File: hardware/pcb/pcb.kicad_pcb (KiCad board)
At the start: 2 copper layers, 26.7 x 56.6 mm, 30 parts, among them J1 L_GPIO, J2 R_GPIO, J3 USB_C_Receptacle_USB2.0_14P, U1 ESP32-C3-WROOM-02, U3 TPS62291

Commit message: I dont remeber, something with PCB :)
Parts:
- BOOT: footprint TestPoint:TestPoint_Pad_2.0x2.0mm -> TestPoint:TestPoint_Pad_D1.5mm
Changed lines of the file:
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@@
 	(net 48 "/SFDLED")
 	(net 49 "/TXLED")
-	(net 50 "Net-(R3-Pad1)")
-	(net 51 "unconnected-(D5-DOUT-Pad2)")
-	(net 52 "Net-(J3-CC1)")
-	(net 53 "Net-(J3-CC2)")
-	(net 54 "Net-(D-RX1-A)")
-	(net 55 "Net-(D-RXOK1-A)")
-	(net 56 "Net-(D-SFD1-A)")
-	(net 57 "Net-(D-TX1-A)")
+	(net 50 "unconnected-(D5-DOUT-Pad2)")
+	(net 51 "Net-(J3-CC1)")
+	(net 52 "Net-(J3-CC2)")
+	(net 53 "Net-(D-RX1-A)")
+	(net 54 "Net-(D-RXOK1-A)")
+	(net 55 "Net-(D-SFD1-A)")
+	(net 56 "Net-(D-TX1-A)")
+	(net 57 "Net-(BOOT1-Pad1)")
 	(footprint "LED_SMD:LED_0402_1005Metric"
 		(layer "F.Cu")
@@
 			(layers "F.Cu" "F.Mask" "F.Paste")
 			(roundrect_rratio 0.25)
-			(net 56 "Net-(D-SFD1-A)")
+			(net 55 "Net-(D-SFD1-A)")
 			(pinfunction "A")
 			(pintype "passive")
@@
 			(layers "F.Cu" "F.Mask" "F.Paste")
 			(roundrect_rratio 0.25)
-			(net 55 "Net-(D-RXOK1-A)")
+			(net 54 "Net-(D-RXOK1-A)")
 			(pinfunction "A")
 			(pintype "passive")
@@
 			(layers "F.Cu" "F.Mask" "F.Paste")
 			(roundrect_rratio 0.1)
-			(net 51 "unconnected-(D5-DOUT-Pad2)")
+			(net 50 "unconnected-(D5-DOUT-Pad2)")
 			(pinfunction "DOUT")
 			(pintype "output")
@@
 			(layers "F.Cu" "F.Mask" "F.Paste")
 			(roundrect_rratio 0.25)
-			(net 52 "Net-(J3-CC1)")
+			(net 51 "Net-(J3-CC1)")
 			(pintype "passive")
 		)
@@
 			(layers "F.Cu" "F.Mask" "F.Paste")
 			(roundrect_rratio 0.25)
-			(net 56 "Net-(D-SFD1-A)")
+			(net 55 "Net-(D-SFD1-A)")
 			(pintype "passive")
 		)
@@
 			(layers "F.Cu" "F.Mask" "F.Paste")
 			(roundrect_rratio 0.25)
-			(net 57 "Net-(D-TX1-A)")
+			(net 56 "Net-(D-TX1-A)")
 			(pinfunction "A")
 			(pintype "passive")
@@
 			(size 0.3 1.24)
 			(layers "F.Cu" "F.Mask" "F.Paste")
-			(net 52 "Net-(J3-CC1)")
+			(net 51 "Net-(J3-CC1)")
 			(pinfunction "CC1")
 			(pintype "bidirectional")
@@
 			(size 0.3 1.24)
 			(layers "F.Cu" "F.Mask" "F.Paste")
-			(net 53 "Net-(J3-CC2)")
+			(net 52 "Net-(J3-CC2)")
 			(pinfunction "CC2")
 			(pintype "bidirectional")
@@
 			(layers "F.Cu" "F.Mask" "F.Paste")
 			(roundrect_rratio 0.25)
-			(net 55 "Net-(D-RXOK1-A)")
+			(net 54 "Net-(D-RXOK1-A)")
 			(pintype "passive")
 		)
@@
 			(layers "F.Cu" "F.Mask" "F.Paste")
 			(roundrect_rratio 0.25)
-			(net 57 "Net-(D-TX1-A)")
+			(net 56 "Net-(D-TX1-A)")
 			(pintype "passive")
 		)
@@
 			(layers "F.Cu" "F.Mask" "F.Paste")
 			(roundrect_rratio 0.25)
-			(net 50 "Net-(R3-Pad1)")
+			(net 57 "Net-(BOOT1-Pad1)")
 			(pintype "passive")
 		)
@@
 			(layers "F.Cu" "F.Mask" "F.Paste")
 			(roundrect_rratio 0.25)
-			(net 54 "Net-(D-RX1-A)")
+			(net 53 "Net-(D-RX1-A)")
 			(pinfunction "A")
 			(pintype "passive")
@@
 			(layers "F.Cu" "F.Mask" "F.Paste")
 			(roundrect_rratio 0.25)
-			(net 53 "Net-(J3-CC2)")
+			(net 52 "Net-(J3-CC2)")
 			(pintype "passive")
 		)
@@
 		)
 	)
-	(footprint "TestPoint:TestPoint_Pad_2.0x2.0mm"
+	(footprint "TestPoint:TestPoint_Pad_D1.5mm"
 		(layer "F.Cu")
 		(at 97.663 66.1924)
-		(descr "SMD rectangular pad as test Point, square 2.0mm side length")
-		(tags "test point SMD pad rectangle square")
+		(descr "SMD pad as test Point, diameter 1.5mm")
+		(tags "test point SMD pad")
 		(property "Reference" "BOOT"
-			(at 0 -1.998 0)
+			(at 0 -1.648 0)
 			(layer "F.SilkS")
 			(effects
@@
 		)
 		(property "Value" "TestPoint"
-			(at 0 2.05 0)
+			(at 0 1.75 0)
 			(layer "F.Fab")
 			(effects
@@
 			)
 		)
-		(property "Datasheet" "~"
+		(property "Datasheet" ""
 			(at 0 0 0)
 			(unlocked yes)
@@
 			)
 		)
-		(property "Description" "test point"
+		(property "Description" ""
 			(at 0 0 0)
 			(unlocked yes)
@@
 		(sheetfile "pcb.kicad_sch")
 		(attr exclude_from_pos_files)
-		(fp_line
-			(start -1.2 -1.2)
-			(end 1.2 -1.2)
-			(stroke
-				(width 0.12)
-				(type solid)
-			)
-			(layer "F.SilkS")
-		)
-		(fp_line
-			(start -1.2 1.2)
-			(end -1.2 -1.2)
-			(stroke
-				(width 0.12)
-				(type solid)
-			)
-			(layer "F.SilkS")
-		)
-		(fp_line
-			(start 1.2 -1.2)
-			(end 1.2 1.2)
-			(stroke
-				(width 0.12)
-				(type solid)
-			)
-			(layer "F.SilkS")
-		)
-		(fp_line
-			(start 1.2 1.2)
-			(end -1.2 1.2)
+		(fp_circle
+			(center 0 0)
+			(end 0 0.95)
 			(stroke
 				(width 0.12)
 				(type solid)
 			)
+			(fill no)
 			(layer "F.SilkS")
 		)
-		(fp_line
-			(start -1.5 -1.5)
-			(end -1.5 1.5)
-			(stroke
-				(width 0.05)
-				(type solid)
-			)
-			(layer "F.CrtYd")
-		)
-		(fp_line
-			(start -1.5 -1.5)
-			(end 1.5 -1.5)
-			(stroke
-				(width 0.05)
-				(type solid)
-			)
-			(layer "F.CrtYd")
-		)
-		(fp_line
-			(start 1.5 1.5)
-			(end -1.5 1.5)
-			(stroke
-				(width 0.05)
-				(type solid)
-			)
-			(layer "F.CrtYd")
-		)
-		(fp_line
-			(start 1.5 1.5)
-			(end 1.5 -1.5)
+		(fp_circle
+			(center 0 0)
+			(end 1.25 0)
 			(stroke
 				(width 0.05)
 				(type solid)
 			)
+			(fill no)
 			(layer "F.CrtYd")
 		)
 		(fp_text user "${REFERENCE}"
-			(at 0 -2 0)
+			(at 0 -1.65 0)
 			(layer "F.Fab")
 			(effects
@@
 			)
 		)
-		(pad "1" smd rect
+		(pad "1" smd circle
 			(at 0 0)
-			(size 2 2)
+			(size 1.5 1.5)
 			(layers "F.Cu" "F.Mask")
-			(net 50 "Net-(R3-Pad1)")
+			(net 57 "Net-(BOOT1-Pad1)")
 			(pinfunction "1")
 			(pintype "passive")
@@
 			(layers "F.Cu" "F.Mask" "F.Paste")
 			(roundrect_rratio 0.25)
-			(net 54 "Net-(D-RX1-A)")
+			(net 53 "Net-(D-RX1-A)")
 			(pintype "passive")
 		)
@@
 	)
 	(segment
-		(start 95.5548 66.296)
-		(end 97.1784 66.296)
-		(width 0.4)
-		(layer "F.Cu")
-		(net 50)
-	)
-	(segment
-		(start 97.282 66.1924)
-		(end 97.663 66.1924)
-		(width 0.4)
-		(layer "F.Cu")
-		(net 50)
-	)
-	(segment
-		(start 97.1784 66.296)
-		(end 97.282 66.1924)
-		(width 0.4)
-		(layer "F.Cu")
-		(net 50)
-	)
-	(segment
 		(start 109.7112 96.0682)
 		(end 108.2702 96.0682)
 		(width 0.2)
 		(layer "F.Cu")
-		(net 52)
+		(net 51)
 	)
 	(segment
@@
 		(width 0.2)
 		(layer "F.Cu")
-		(net 52)
+		(net 51)
 	)
 	(segment
@@
 		(width 0.2)
 		(layer "F.Cu")
-		(net 53)
+		(net 52)
 	)
 	(segment
@@
 		(width 0.2)
 		(layer "F.Cu")
-		(net 53)
+		(net 52)
 	)
 	(segment
@@
 		(width 0.4)
 		(layer "F.Cu")
-		(net 54)
+		(net 53)
 	)
 	(segment
@@
 		(width 0.4)
 		(layer "F.Cu")
-		(net 55)
+		(net 54)
 	)
 	(segment
@@
 		(width 0.4)
 		(layer "F.Cu")
-		(net 56)
+		(net 55)
 	)
 	(segment
@@
 		(width 0.4)
 		(layer "F.Cu")
+		(net 56)
+	)
+	(segment
+		(start 95.5548 66.296)
+		(end 97.1784 66.296)
+		(width 0.4)
+		(layer "F.Cu")
+		(net 57)
+	)
+	(segment
+		(start 97.282 66.1924)
+		(end 97.663 66.1924)
+		(width 0.4)
+		(layer "F.Cu")
+		(net 57)
+	)
+	(segment
+		(start 97.1784 66.296)
+		(end 97.282 66.1924)
+		(width 0.4)
+		(layer "F.Cu")

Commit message: add neeko
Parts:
- moved BOOT1 1.93 mm to (98.7, 67.8)
- moved R2 1.80 mm to (101.7, 65.8)
- moved R4 1.80 mm to (101.7, 68.3)
- renumbered BOOT to BOOT1, D-RX to D-RX1, D-RXOK to D-RXOK1, D-SFD to D-SFD1, D-TX to D-TX1, DWM to DWM1, MODE to MODE1, RESET to RESET1
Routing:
- net Net-(U1-IO8): track 8.45 -> 11.7 mm
- net Net-(U1-IO2): track 23.0 -> 21.3 mm
- net Net-(BOOT1-Pad1): track 2.15 -> 3.78 mm
- net +3V3: track 119.7 -> 121.2 mm
- net /U-IRQ: track 48.8 -> 47.8 mm
- net GND: vias 13 -> 14
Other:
- board text added: "${REFERENCE}"
- board text added: "D-RX"
- board text added: "D-RXOK"
- board text added: "D-SFD"
- board text added: "D-TX"
- board text added: "DWM"
- board text added: "MODE"
- board text added: "RESET"

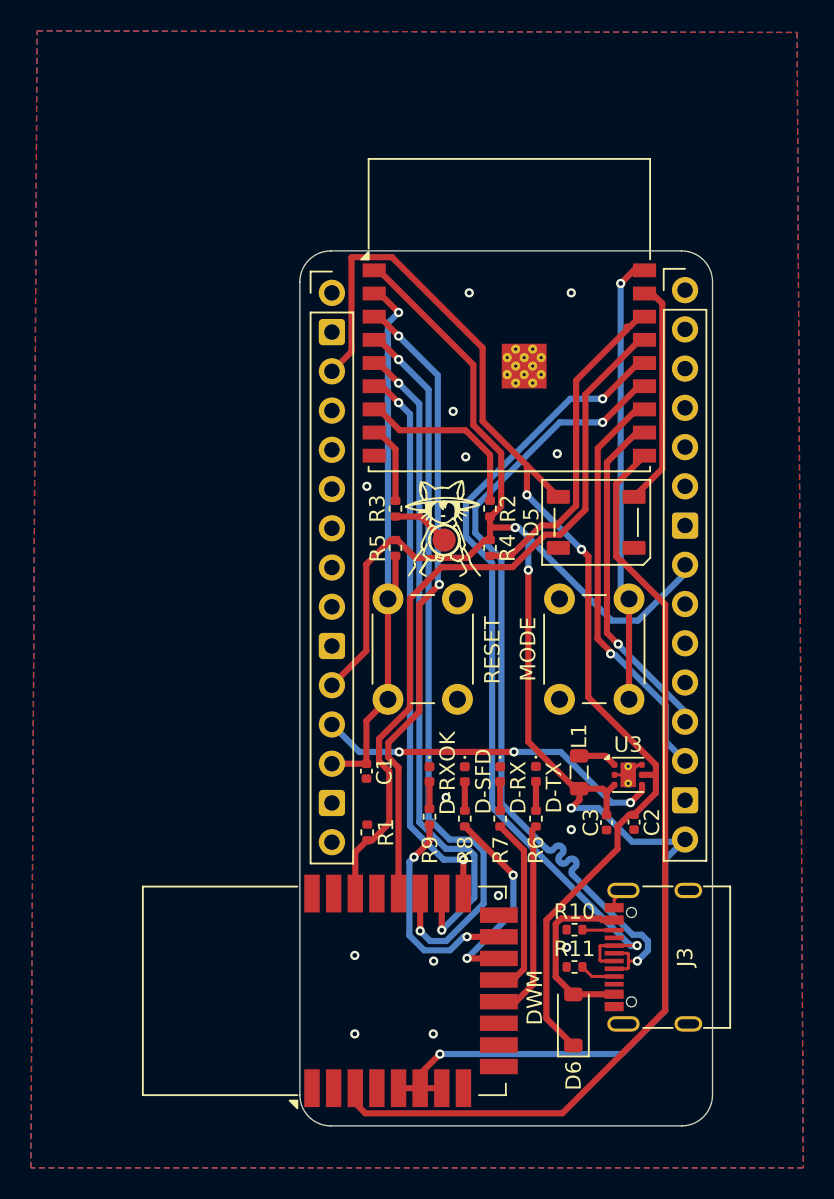
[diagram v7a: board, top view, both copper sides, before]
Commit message: reroute dálnice for backlit lightbulb
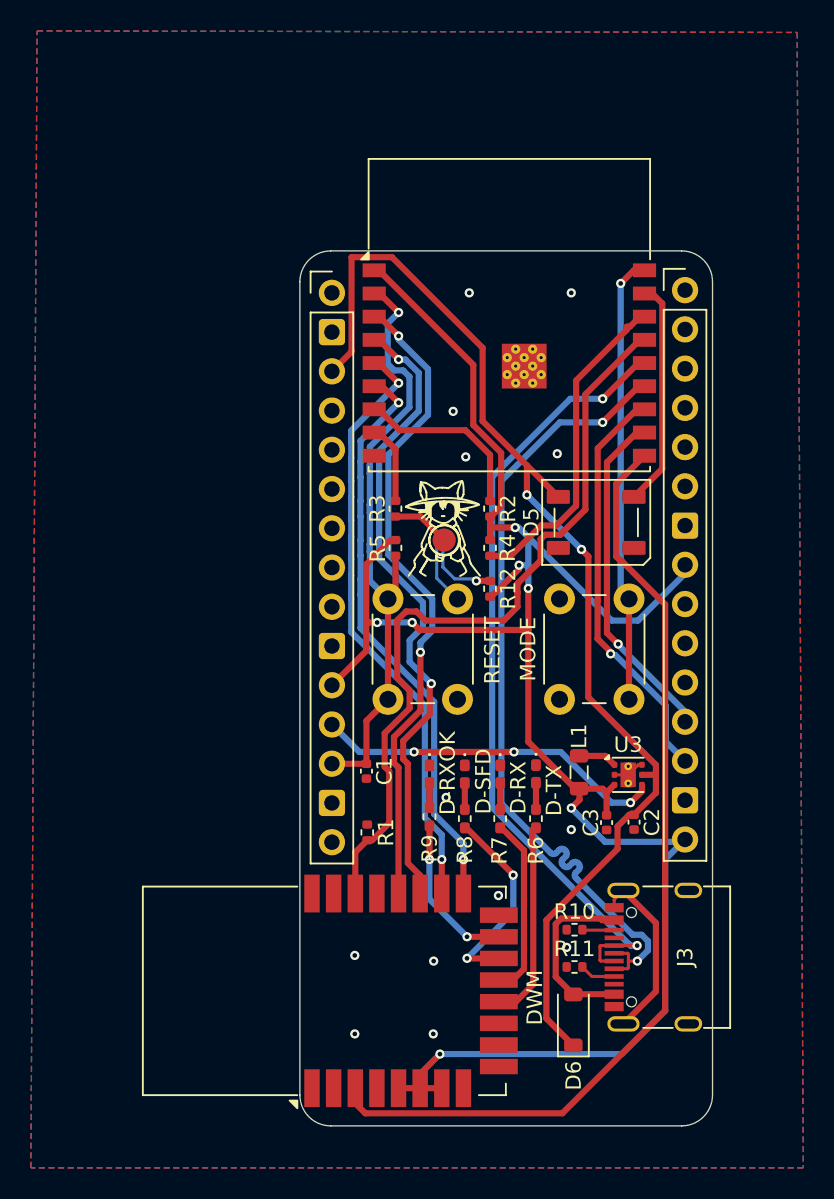
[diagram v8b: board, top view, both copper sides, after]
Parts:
- added D1: LED, LED_SMD:LED_0201_0603Metric_Pad0.64x0.40mm_HandSolder, B.Cu at (98.7, 67.8)
- added R12: R, Resistor_SMD:R_0402_1005Metric, F.Cu at (101.7, 71.0)
- D-RX1, D-RXOK1, D-SFD1, D-TX1: footprint LED_SMD:LED_0402_1005Metric -> LED_SMD:LED_0402_1005Metric_Pad0.77x0.64mm_HandSolder
- R6, R7, R8, R9: footprint Resistor_SMD:R_0402_1005Metric -> Resistor_SMD:R_0402_1005Metric_Pad0.72x0.64mm_HandSolder
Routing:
- net GND: track 3.41 -> 18.2 mm, vias 14 -> 13
- net +3V3: track 121.2 -> 128.4 mm, vias 4 -> 7
- net /U-SPIMISO: track 48.2 -> 42.0 mm
- net Net-(D1-A): track 0.00 -> 5.40 mm, vias 0 -> 1
- net /U-SPIMOSI: track 43.6 -> 38.9 mm
- net /RXOKLED: track 14.3 -> 10.3 mm
- net /ENABLE: track 38.0 -> 40.4 mm
- net /U-IRQ: track 47.8 -> 50.0 mm
- net /U-SPICLK: track 40.9 -> 42.4 mm
- net USB_D+: track 53.1 -> 51.7 mm
- net USB_D-: track 54.4 -> 53.0 mm
- net /U-SPICSn: track 36.3 -> 37.6 mm
